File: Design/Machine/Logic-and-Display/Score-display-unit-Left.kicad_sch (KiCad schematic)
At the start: 5 parts, among them M1 Red, M2 Red, M3 Red, M4 Red

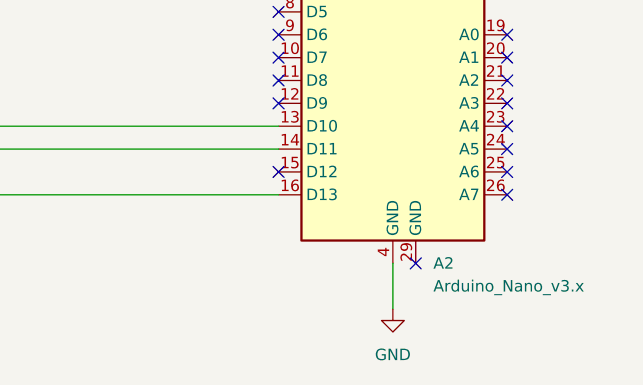
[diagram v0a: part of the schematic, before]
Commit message: fix: scores MCU GNDs
connect all Nano's GNDs to GND on right and left score schematics
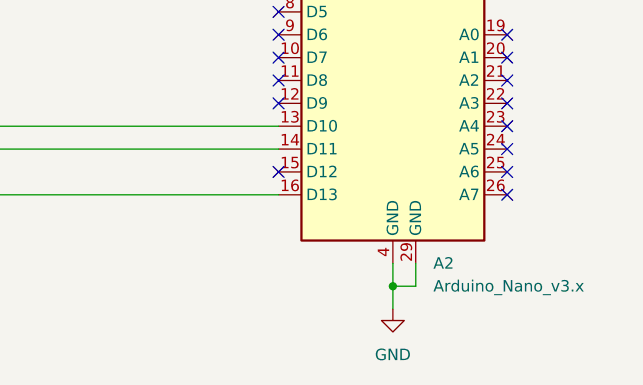
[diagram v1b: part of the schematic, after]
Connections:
- net GND: now also A2.29 (GND)
- no-connect marks 29 -> 28
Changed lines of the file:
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@@
     (rev "1.0")
+  )
+  (junction (at 205.74 127) (diameter 0) (color 0 0 0 0)
   )
   (no_connect (at 218.44 93.98))
@@
   (no_connect (at 218.44 114.3))
   (no_connect (at 193.04 93.98))
-  (no_connect (at 208.28 124.46))
   (no_connect (at 210.82 73.66))
   (no_connect (at 160.02 96.52))
@@
     (stroke (width 0) (type default))
   )
+  (wire (pts (xy 208.28 127) (xy 205.74 127))
+    (stroke (width 0) (type default))
+  )
   (wire (pts (xy 53.34 111.76) (xy 53.34 91.44))
     (stroke (width 0) (type default))
   )
+  (wire (pts (xy 205.74 127) (xy 205.74 129.54))
+    (stroke (width 0) (type default))
+  )
   (wire (pts (xy 106.68 88.9) (xy 114.3 88.9))
+    (stroke (width 0) (type default))
+  )
+  (wire (pts (xy 208.28 124.46) (xy 208.28 127))
     (stroke (width 0) (type default))
   )
@@
     (stroke (width 0) (type default))
   )
-  (wire (pts (xy 205.74 124.46) (xy 205.74 129.54))
+  (wire (pts (xy 205.74 124.46) (xy 205.74 127))
     (stroke (width 0) (type default))
   )

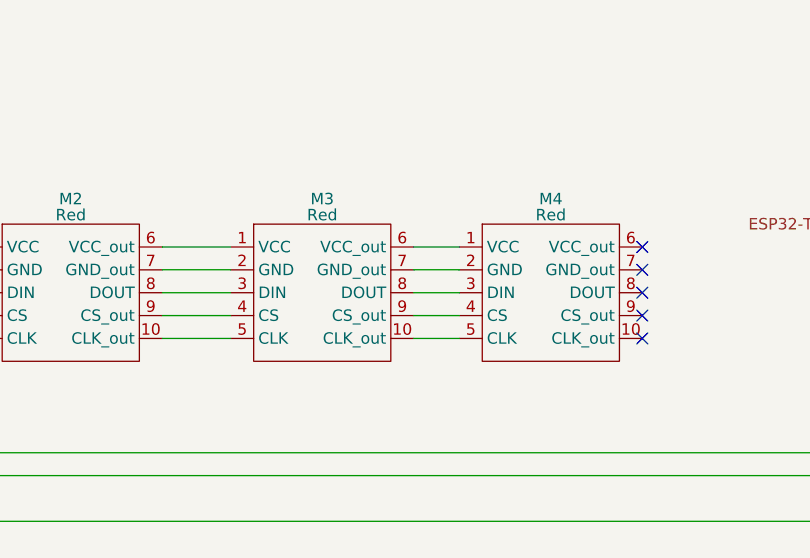
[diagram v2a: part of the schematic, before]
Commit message: feat: display units schematics
complete all display units schematics, this is left and right scores units; and LEDs, timer, and period display unit
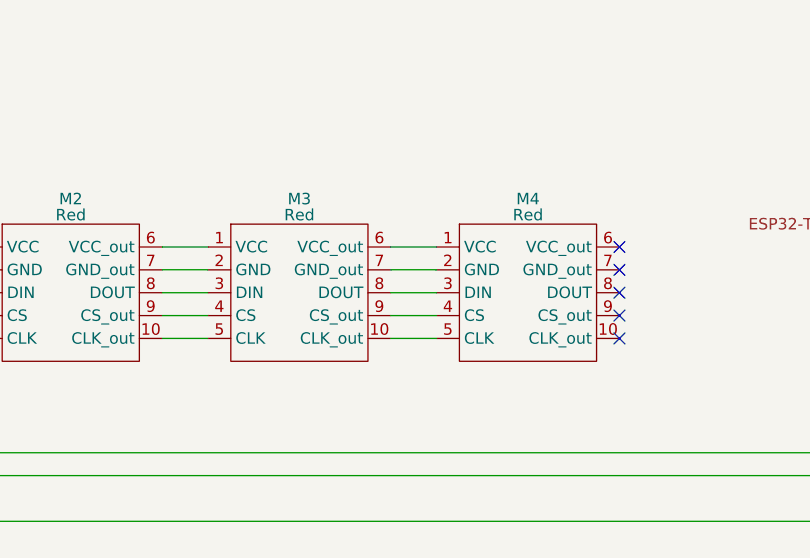
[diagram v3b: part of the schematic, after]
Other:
- title: (none) -> Left score display unit schematic
- moved on the sheet: M3, M4
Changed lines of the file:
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@@
   (paper "A4")
   (title_block
+    (title "Left score display unit schematic")
     (date "2023-05-19")
-    (rev "1.0")
+    (rev "1.0.0")
+    (comment 1 "Connection to logic unit pending")
   )
   (junction (at 205.74 127) (diameter 0) (color 0 0 0 0)
   )
   (no_connect (at 218.44 93.98))
-  (no_connect (at 160.02 86.36))
+  (no_connect (at 157.48 86.36))
   (no_connect (at 218.44 116.84))
   (no_connect (at 193.04 88.9))
@@
   (no_connect (at 218.44 109.22))
   (no_connect (at 218.44 99.06))
-  (no_connect (at 160.02 93.98))
+  (no_connect (at 157.48 93.98))
   (no_connect (at 218.44 83.82))
   (no_connect (at 218.44 104.14))
@@
   (no_connect (at 218.44 106.68))
   (no_connect (at 218.44 101.6))
-  (no_connect (at 160.02 88.9))
+  (no_connect (at 157.48 88.9))
   (no_connect (at 193.04 86.36))
   (no_connect (at 218.44 111.76))
@@
   (no_connect (at 193.04 93.98))
   (no_connect (at 210.82 73.66))
-  (no_connect (at 160.02 96.52))
+  (no_connect (at 157.48 96.52))
   (no_connect (at 218.44 86.36))
-  (no_connect (at 160.02 91.44))
+  (no_connect (at 157.48 91.44))
   (no_connect (at 193.04 104.14))
   (no_connect (at 193.04 101.6))
@@
     (stroke (width 0) (type default))
   )
-  (wire (pts (xy 106.68 91.44) (xy 114.3 91.44))
+  (wire (pts (xy 106.68 91.44) (xy 111.76 91.44))
     (stroke (width 0) (type default))
   )
@@
     (stroke (width 0) (type default))
   )
-  (wire (pts (xy 106.68 88.9) (xy 114.3 88.9))
+  (wire (pts (xy 106.68 88.9) (xy 111.76 88.9))
     (stroke (width 0) (type default))
   )
@@
     (stroke (width 0) (type default))
   )
-  (wire (pts (xy 134.62 93.98) (xy 139.7 93.98))
-    (stroke (width 0) (type default))
-  )
-  (wire (pts (xy 134.62 88.9) (xy 139.7 88.9))
-    (stroke (width 0) (type default))
-  )
-  (wire (pts (xy 134.62 91.44) (xy 139.7 91.44))
+  (wire (pts (xy 132.08 93.98) (xy 137.16 93.98))
+    (stroke (width 0) (type default))
+  )
+  (wire (pts (xy 132.08 88.9) (xy 137.16 88.9))
+    (stroke (width 0) (type default))
+  )
+  (wire (pts (xy 132.08 91.44) (xy 137.16 91.44))
     (stroke (width 0) (type default))
   )
@@
     (stroke (width 0) (type default))
   )
-  (wire (pts (xy 106.68 93.98) (xy 114.3 93.98))
+  (wire (pts (xy 106.68 93.98) (xy 111.76 93.98))
     (stroke (width 0) (type default))
   )
@@
     (stroke (width 0) (type default))
   )
-  (wire (pts (xy 106.68 96.52) (xy 114.3 96.52))
+  (wire (pts (xy 106.68 96.52) (xy 111.76 96.52))
     (stroke (width 0) (type default))
   )
@@
     (stroke (width 0) (type default))
   )
-  (wire (pts (xy 134.62 86.36) (xy 139.7 86.36))
-    (stroke (width 0) (type default))
-  )
-  (wire (pts (xy 134.62 96.52) (xy 139.7 96.52))
+  (wire (pts (xy 132.08 86.36) (xy 137.16 86.36))
+    (stroke (width 0) (type default))
+  )
+  (wire (pts (xy 132.08 96.52) (xy 137.16 96.52))
     (stroke (width 0) (type default))
   )
@@
     (stroke (width 0) (type default))
   )
-  (wire (pts (xy 106.68 86.36) (xy 114.3 86.36))
+  (wire (pts (xy 106.68 86.36) (xy 111.76 86.36))
     (stroke (width 0) (type default))
   )
@@
     )
   )
-  (symbol (lib_id "Arduino modules:8x8_LED_Matrix_MAX7219") (at 124.46 81.28 0) (unit 1)
+  (symbol (lib_id "Arduino modules:8x8_LED_Matrix_MAX7219") (at 121.92 81.28 0) (unit 1)
     (in_bom yes) (on_board yes) (dnp no)
-    (property "Reference" "M3" (at 124.46 81.026 0)
-      (effects (font (size 1.27 1.27)))
-    )
-    (property "Value" "Red" (at 124.46 82.804 0)
-      (effects (font (size 1.27 1.27)))
-    )
-    (property "Footprint" "" (at 124.46 81.28 0)
-      (effects (font (size 1.27 1.27)) hide)
-    )
-    (property "Datasheet" "" (at 124.46 81.28 0)
+    (property "Reference" "M3" (at 121.92 81.026 0)
+      (effects (font (size 1.27 1.27)))
+    )
+    (property "Value" "Red" (at 121.92 82.804 0)
+      (effects (font (size 1.27 1.27)))
+    )
+    (property "Footprint" "" (at 121.92 81.28 0)
+      (effects (font (size 1.27 1.27)) hide)
+    )
+    (property "Datasheet" "" (at 121.92 81.28 0)
       (effects (font (size 1.27 1.27)) hide)
     )
@@
     )
   )
-  (symbol (lib_id "Arduino modules:8x8_LED_Matrix_MAX7219") (at 149.86 81.28 0) (unit 1)
+  (symbol (lib_id "Arduino modules:8x8_LED_Matrix_MAX7219") (at 147.32 81.28 0) (unit 1)
     (in_bom yes) (on_board yes) (dnp no)
-    (property "Reference" "M4" (at 149.86 81.026 0)
-      (effects (font (size 1.27 1.27)))
-    )
-    (property "Value" "Red" (at 149.86 82.804 0)
-      (effects (font (size 1.27 1.27)))
-    )
-    (property "Footprint" "" (at 149.86 81.28 0)
-      (effects (font (size 1.27 1.27)) hide)
-    )
-    (property "Datasheet" "" (at 149.86 81.28 0)
-      (effects (font (size 1.27 1.27)) hide)
-    )
+    (property "Reference" "M4" (at 147.32 81.026 0)
+      (effects (font (size 1.27 1.27)))
+    )
+    (property "Value" "Red" (at 147.32 82.804 0)
+      (effects (font (size 1.27 1.27)))
+    )
+    (property "Footprint" "" (at 147.32 81.28 0)
+      (effects (font (size 1.27 1.27)) hide)
+    )
+    (property "Datasheet" "" (at 147.32 81.28 0)
+      (effects (font (size 1.27 1.27)) hide)
+    )

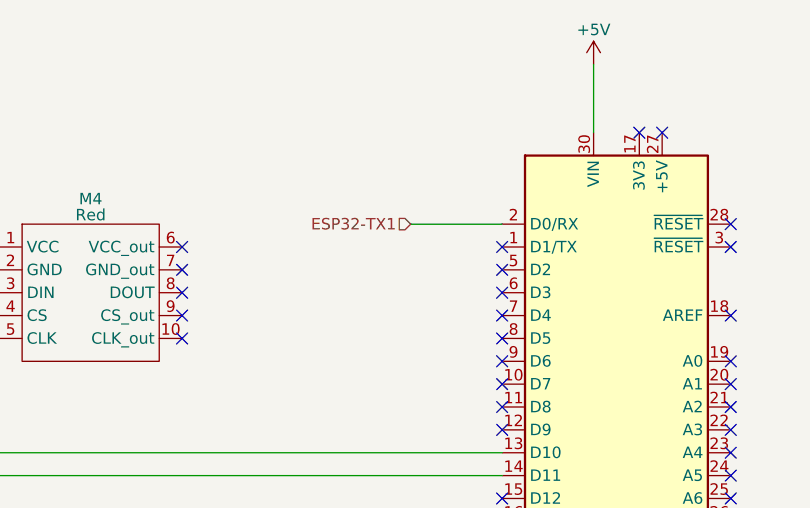
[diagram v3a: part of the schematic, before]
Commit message: feat: logic unit schematics
make schematics for logic unit, power redundancy unit still missing
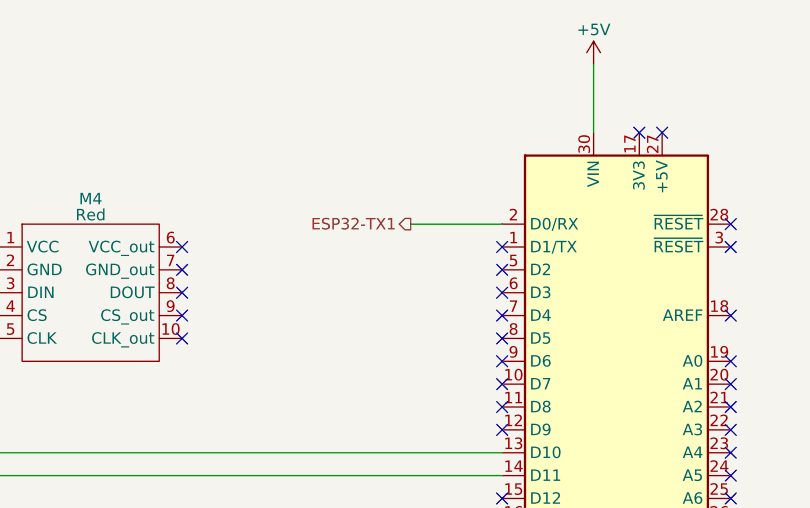
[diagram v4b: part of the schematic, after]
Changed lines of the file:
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@@
     (stroke (width 0) (type default))
   )
-  (hierarchical_label "ESP32-TX1" (shape input) (at 182.88 83.82 180) (fields_autoplaced)
+  (hierarchical_label "ESP32-TX1" (shape output) (at 182.88 83.82 180) (fields_autoplaced)
     (effects (font (size 1.27 1.27)) (justify right))
   )
